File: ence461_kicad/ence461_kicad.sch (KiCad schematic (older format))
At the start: 54 parts, among them U1 LMV324, U2 LMV324, U3 LMV324, U4 74HC3G14DP, U5 LMV321

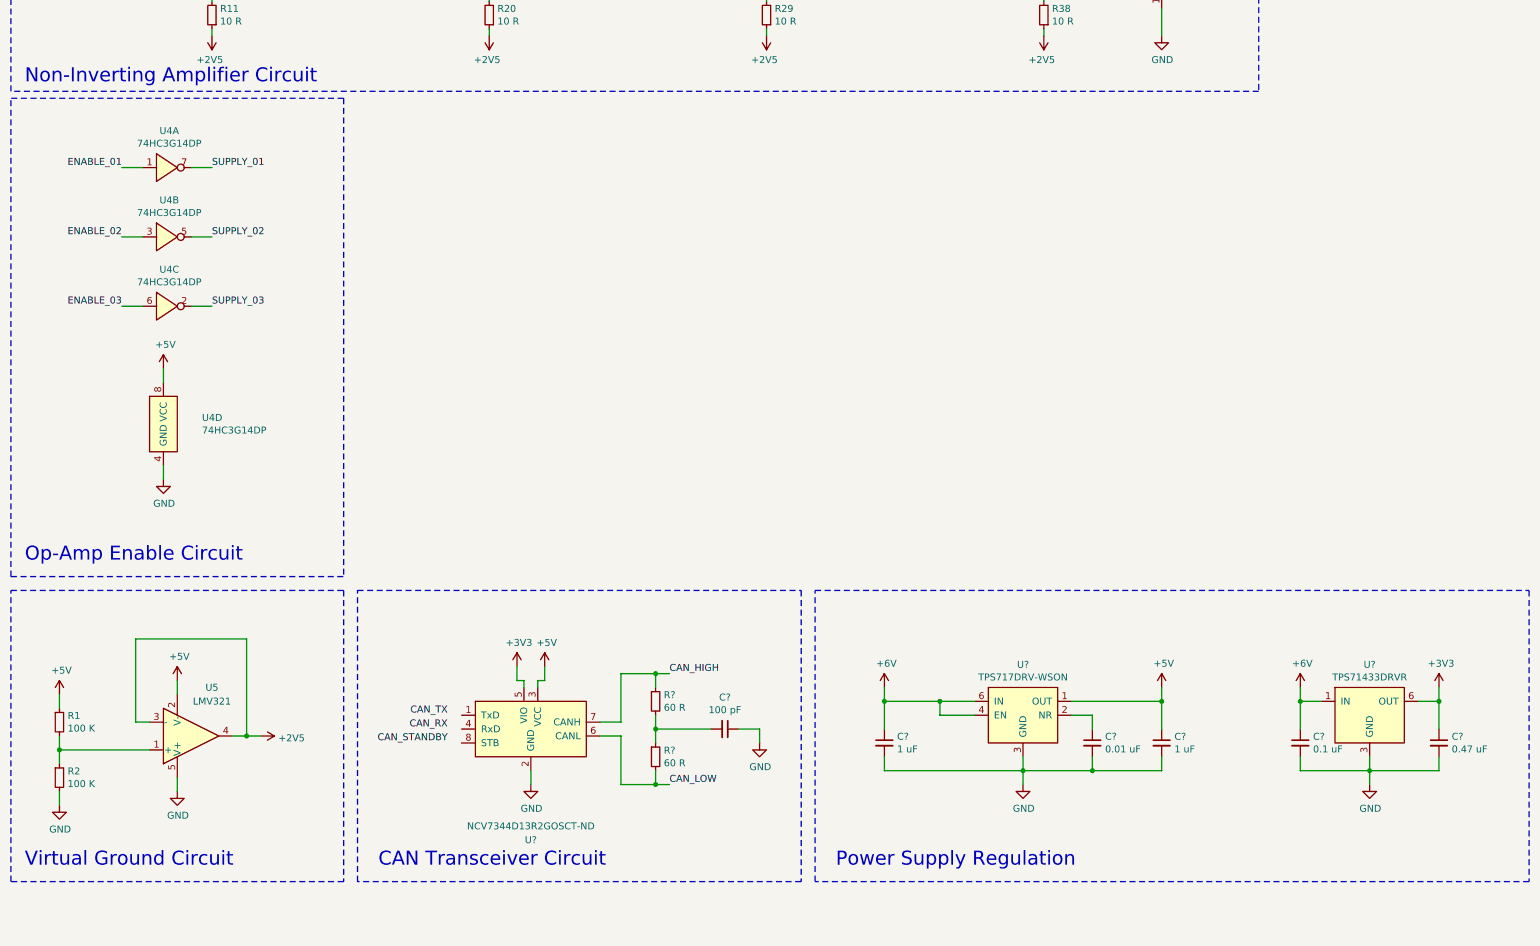
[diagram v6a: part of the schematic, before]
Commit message: Added stubs for external connectors.
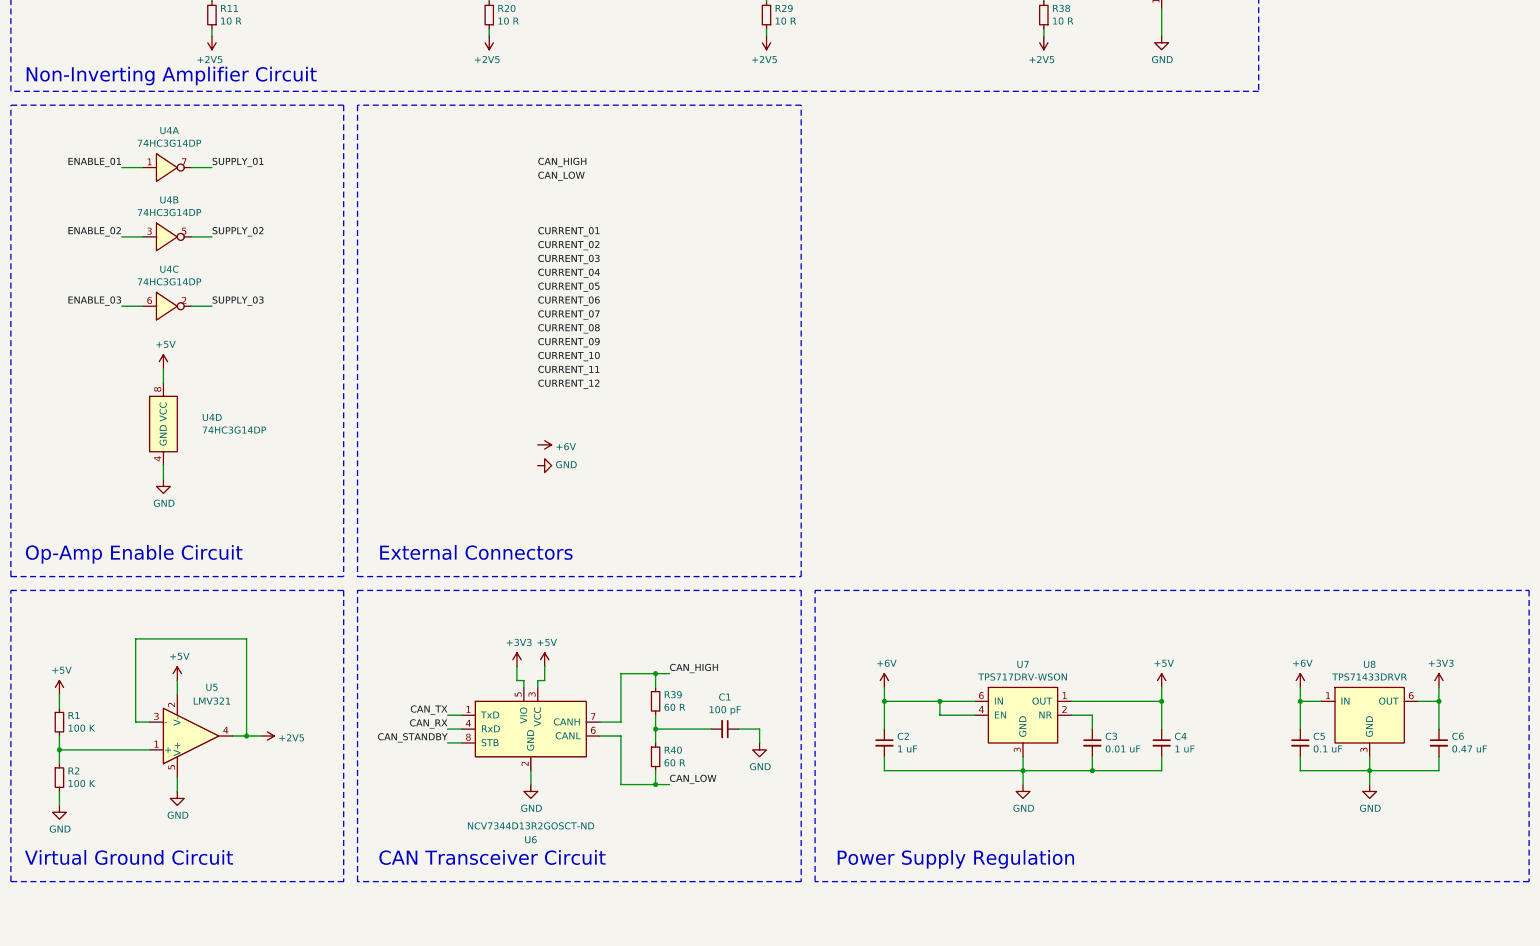
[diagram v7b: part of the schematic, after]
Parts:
- gave numbers to parts that had none: 11
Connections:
- net CAN_RX: now also U6.4 (RxD)
- net CAN_STANDBY: now also U6.8 (STB)
- net CAN_TX: now also U6.1 (TxD)
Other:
- note added: "External Connectors"
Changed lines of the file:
@@
 encoding utf-8
 Sheet 1 1
-Title ""
-Date ""
-Rev ""
+Title "Current Sense Slave"
+Date "2020-05-23"
+Rev "1"
 Comp ""
 Comment1 ""
@@
 	8150 5050 8150 5000
 Wire Notes Line
-	3100 5500 3100 8950
-Wire Notes Line
-	700  8950 700  5500
+	3100 5550 3100 8950
+Wire Notes Line
+	700  8950 700  5550
 Text Notes 800  8850 0    101  ~ 0
 Op-Amp Enable Circuit
@@
 	700  8950 3100 8950
 Wire Notes Line
-	3100 5500 700  5500
+	3100 5550 700  5550
 Text Label 9000 950  0    50   ~ 0
 SUPPLY_01
@@
 SUPPLY_03
 $Comp
-L ence461_symbol_library:NCV7344D13R2GOSCT-ND U?
+L ence461_symbol_library:NCV7344D13R2GOSCT-ND U6
 U 1 1 5EEFE06C
 P 4450 9350
-F 0 "U?" H 4450 7850 50  0000 C CNN
+F 0 "U6" H 4450 7850 50  0000 C CNN
 F 1 "NCV7344D13R2GOSCT-ND" H 4450 7950 50  0000 C CNN
 F 2 "Package_SO:SOIC-8_3.9x4.9mm_P1.27mm" H 4450 9350 50  0001 C CNN
@@
 $EndComp
 $Comp
-L power:+5V #PWR?
+L power:+5V #PWR027
 U 1 1 5EEFF4F9
 P 4550 9600
-F 0 "#PWR?" H 4550 9450 50  0001 C CNN
+F 0 "#PWR027" H 4550 9450 50  0001 C CNN
 F 1 "+5V" H 4565 9773 50  0000 C CNN
 F 2 "" H 4550 9600 50  0001 C CNN
@@
 $EndComp
 $Comp
-L power:+3V3 #PWR?
+L power:+3V3 #PWR023
 U 1 1 5EEFF85C
 P 4350 9600
-F 0 "#PWR?" H 4350 9450 50  0001 C CNN
+F 0 "#PWR023" H 4350 9450 50  0001 C CNN
 F 1 "+3V3" H 4365 9773 50  0000 C CNN
 F 2 "" H 4350 9600 50  0001 C CNN
@@
 $EndComp
 $Comp
-L power:GND #PWR?
+L power:GND #PWR024
 U 1 1 5EF006FA
 P 4450 10450
-F 0 "#PWR?" H 4450 10200 50  0001 C CNN
+F 0 "#PWR024" H 4450 10200 50  0001 C CNN
 F 1 "GND" H 4455 10277 50  0000 C CNN
 F 2 "" H 4450 10450 50  0001 C CNN
@@
 CAN_LOW
 $Comp
-L Device:R_Small R?
+L Device:R_Small R39
 U 1 1 5EF1902E
 P 5350 9850
-F 0 "R?" H 5409 9896 50  0000 L CNN
+F 0 "R39" H 5409 9896 50  0000 L CNN
 F 1 "60 R" H 5409 9805 50  0000 L CNN
 F 2 "" H 5350 9850 50  0001 C CNN
@@
 $EndComp
 $Comp
-L Device:R_Small R?
+L Device:R_Small R40
 U 1 1 5EF1939D
 P 5350 10250
-F 0 "R?" H 5409 10296 50  0000 L CNN
+F 0 "R40" H 5409 10296 50  0000 L CNN
 F 1 "60 R" H 5409 10205 50  0000 L CNN
 F 2 "" H 5350 10250 50  0001 C CNN
@@
 $EndComp
 $Comp
-L Device:C_Small C?
+L Device:C_Small C1
 U 1 1 5EF1A392
 P 5850 10050
-F 0 "C?" V 5621 10050 50  0000 C CNN
+F 0 "C1" V 5621 10050 50  0000 C CNN
 F 1 "100 pF" V 5712 10050 50  0000 C CNN
 F 2 "" H 5850 10050 50  0001 C CNN
@@
 $EndComp
 $Comp
-L power:GND #PWR?
+L power:GND #PWR028
 U 1 1 5EF1A94A
 P 6100 10150
-F 0 "#PWR?" H 6100 9900 50  0001 C CNN
+F 0 "#PWR028" H 6100 9900 50  0001 C CNN
 F 1 "GND" H 6105 9977 50  0000 C CNN
 F 2 "" H 6100 10150 50  0001 C CNN
@@
 CAN Transceiver Circuit
 $Comp
-L ence461_symbol_library:TPS717DRV-WSON U?
+L ence461_symbol_library:TPS717DRV-WSON U7
 U 1 1 5F0550EF
 P 8000 9700
-F 0 "U?" H 8000 9815 50  0000 C CNN
+F 0 "U7" H 8000 9815 50  0000 C CNN
 F 1 "TPS717DRV-WSON" H 8000 9724 50  0000 C CNN
 F 2 "Package_SON:WSON-6-1EP_2x2mm_P0.65mm_EP1x1.6mm_ThermalVias" H 8000 9700 50  0001 C CNN
@@
 $EndComp
 $Comp
-L power:GND #PWR?
+L power:GND #PWR030
 U 1 1 5F0554ED
 P 8000 10450
-F 0 "#PWR?" H 8000 10200 50  0001 C CNN
+F 0 "#PWR030" H 8000 10200 50  0001 C CNN
 F 1 "GND" H 8005 10277 50  0000 C CNN
 F 2 "" H 8000 10450 50  0001 C CNN
@@
 $EndComp
 $Comp
-L Device:C_Small C?
+L Device:C_Small C3
 U 1 1 5F05E77E
 P 8500 10150
-F 0 "C?" H 8592 10196 50  0000 L CNN
+F 0 "C3" H 8592 10196 50  0000 L CNN
 F 1 "0.01 uF" H 8592 10105 50  0000 L CNN
 F 2 "" H 8500 10150 50  0001 C CNN
@@
 $EndComp
 $Comp
-L Device:C_Small C?
+L Device:C_Small C2
 U 1 1 5F05EC29
 P 7000 10150
-F 0 "C?" H 7092 10196 50  0000 L CNN
+F 0 "C2" H 7092 10196 50  0000 L CNN
 F 1 "1 uF" H 7092 10105 50  0000 L CNN
 F 2 "" H 7000 10150 50  0001 C CNN
@@
 $EndComp
 $Comp
-L Device:C_Small C?
+L Device:C_Small C4
 U 1 1 5F05F1F3
 P 9000 10150
-F 0 "C?" H 9092 10196 50  0000 L CNN
+F 0 "C4" H 9092 10196 50  0000 L CNN
 F 1 "1 uF" H 9092 10105 50  0000 L CNN
 F 2 "" H 9000 10150 50  0001 C CNN
@@
 	7400 9850 7000 9850
 $Comp
-L power:+6V #PWR?
+L power:+6V #PWR029
 U 1 1 5F0FB207
 P 7000 9750
-F 0 "#PWR?" H 7000 9600 50  0001 C CNN
+F 0 "#PWR029" H 7000 9600 50  0001 C CNN
 F 1 "+6V" H 7015 9923 50  0000 C CNN
 F 2 "" H 7000 9750 50  0001 C CNN
@@
 $EndComp
 $Comp
-L power:+5V #PWR?
+L power:+5V #PWR031
 U 1 1 5F0FB4D8
 P 9000 9750
-F 0 "#PWR?" H 9000 9600 50  0001 C CNN
+F 0 "#PWR031" H 9000 9600 50  0001 C CNN
 F 1 "+5V" H 9015 9923 50  0000 C CNN
 F 2 "" H 9000 9750 50  0001 C CNN
@@
 Connection ~ 7000 9850
 $Comp
-L ence461_symbol_library:TPS71433DRVR U?
+L ence461_symbol_library:TPS71433DRVR U8
 U 1 1 5F130B93
 P 10500 9700
-F 0 "U?" H 10500 9815 50  0000 C CNN
+F 0 "U8" H 10500 9815 50  0000 C CNN
 F 1 "TPS71433DRVR" H 10500 9724 50  0000 C CNN
 F 2 "Package_SON:WSON-6-1EP_2x2mm_P0.65mm_EP1x1.6mm" H 10500 9700 50  0001 C CNN
@@
 $EndComp
 $Comp
-L Device:C_Small C?
+L Device:C_Small C5
 U 1 1 5F1319AF
 P 10000 10150
-F 0 "C?" H 10092 10196 50  0000 L CNN
+F 0 "C5" H 10092 10196 50  0000 L CNN
 F 1 "0.1 uF" H 10092 10105 50  0000 L CNN
 F 2 "" H 10000 10150 50  0001 C CNN
@@
 $EndComp
 $Comp
-L Device:C_Small C?
+L Device:C_Small C6
 U 1 1 5F131C86
 P 11000 10150
-F 0 "C?" H 11092 10196 50  0000 L CNN
+F 0 "C6" H 11092 10196 50  0000 L CNN
 F 1 "0.47 uF" H 11092 10105 50  0000 L CNN
 F 2 "" H 11000 10150 50  0001 C CNN
@@
 Connection ~ 10500 10350
 $Comp
-L power:GND #PWR?
+L power:GND #PWR033
 U 1 1 5F1611CF
 P 10500 10450
-F 0 "#PWR?" H 10500 10200 50  0001 C CNN
+F 0 "#PWR033" H 10500 10200 50  0001 C CNN
 F 1 "GND" H 10505 10277 50  0000 C CNN
 F 2 "" H 10500 10450 50  0001 C CNN
@@
 	10500 10450 10500 10350
 $Comp
-L power:+3V3 #PWR?
+L power:+3V3 #PWR034
 U 1 1 5F16C988
 P 11000 9750
-F 0 "#PWR?" H 11000 9600 50  0001 C CNN
+F 0 "#PWR034" H 11000 9600 50  0001 C CNN
 F 1 "+3V3" H 11015 9923 50  0000 C CNN
 F 2 "" H 11000 9750 50  0001 C CNN
@@
 Connection ~ 11000 9850
 $Comp
-L power:+6V #PWR?
+L power:+6V #PWR032
 U 1 1 5F1792AF
 P 10000 9750
-F 0 "#PWR?" H 10000 9600 50  0001 C CNN
+F 0 "#PWR032" H 10000 9600 50  0001 C CNN
 F 1 "+6V" H 10015 9923 50  0000 C CNN
 F 2 "" H 10000 9750 50  0001 C CNN
@@
 Text Notes 6650 11050 0    101  ~ 0
 Power Supply Regulation
+Wire Wire Line
+	3850 9950 3950 9950
+Wire Wire Line
+	3850 10050 3950 10050
+Wire Wire Line
+	3850 10150 3950 10150
+Text Label 4500 6000 0    50   ~ 0
+CAN_HIGH
+Text Label 4500 6100 0    50   ~ 0
+CAN_LOW
+Text Label 4500 6500 0    50   ~ 0
+CURRENT_01
+Text Label 4500 6600 0    50   ~ 0
+CURRENT_02
+Text Label 4500 6700 0    50   ~ 0
+CURRENT_03
+Text Label 4500 6800 0    50   ~ 0
+CURRENT_04
+Text Label 4500 6900 0    50   ~ 0
+CURRENT_05
+Text Label 4500 7000 0    50   ~ 0
+CURRENT_06
+Text Label 4500 7100 0    50   ~ 0
+CURRENT_07
+Text Label 4500 7200 0    50   ~ 0
+CURRENT_08
+Text Label 4500 7300 0    50   ~ 0
+CURRENT_09
+Text Label 4500 7400 0    50   ~ 0
+CURRENT_10
+Text Label 4500 7500 0    50   ~ 0
+CURRENT_11
+Text Label 4500 7600 0    50   ~ 0
+CURRENT_12
+$Comp
+L power:+6V #PWR025
+U 1 1 5F1EDB8B
+P 4500 8000
+F 0 "#PWR025" H 4500 7850 50  0001 C CNN
+F 1 "+6V" V 4515 8128 50  0000 L CNN
+F 2 "" H 4500 8000 50  0001 C CNN
+F 3 "" H 4500 8000 50  0001 C CNN
+	1    4500 8000
+	0    1    1    0
+$EndComp
+$Comp
+L power:GND #PWR026
+U 1 1 5F1EE14E
+P 4500 8150
+F 0 "#PWR026" H 4500 7900 50  0001 C CNN
+F 1 "GND" V 4505 8022 50  0000 R CNN
+F 2 "" H 4500 8150 50  0001 C CNN
+F 3 "" H 4500 8150 50  0001 C CNN
+	1    4500 8150
+	0    -1   -1   0
+$EndComp
+Wire Notes Line
+	6400 8950 6400 5550
+Wire Notes Line
+	6400 5550 3200 5550
+Wire Notes Line
+	3200 5550 3200 8950
+Wire Notes Line
+	3200 8950 6400 8950
+Text Notes 3350 8850 0    101  ~ 0
+External Connectors
 $EndSCHEMATC
